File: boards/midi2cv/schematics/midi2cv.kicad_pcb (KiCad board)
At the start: 2 copper layers, 83 x 69 mm, 49 parts, among them J1 Jack-DC (12-32V), U1 LM7805_TO220, U2 6N138, U3 LM358, U4 MCP4822, U5 Pico, U6 LM358

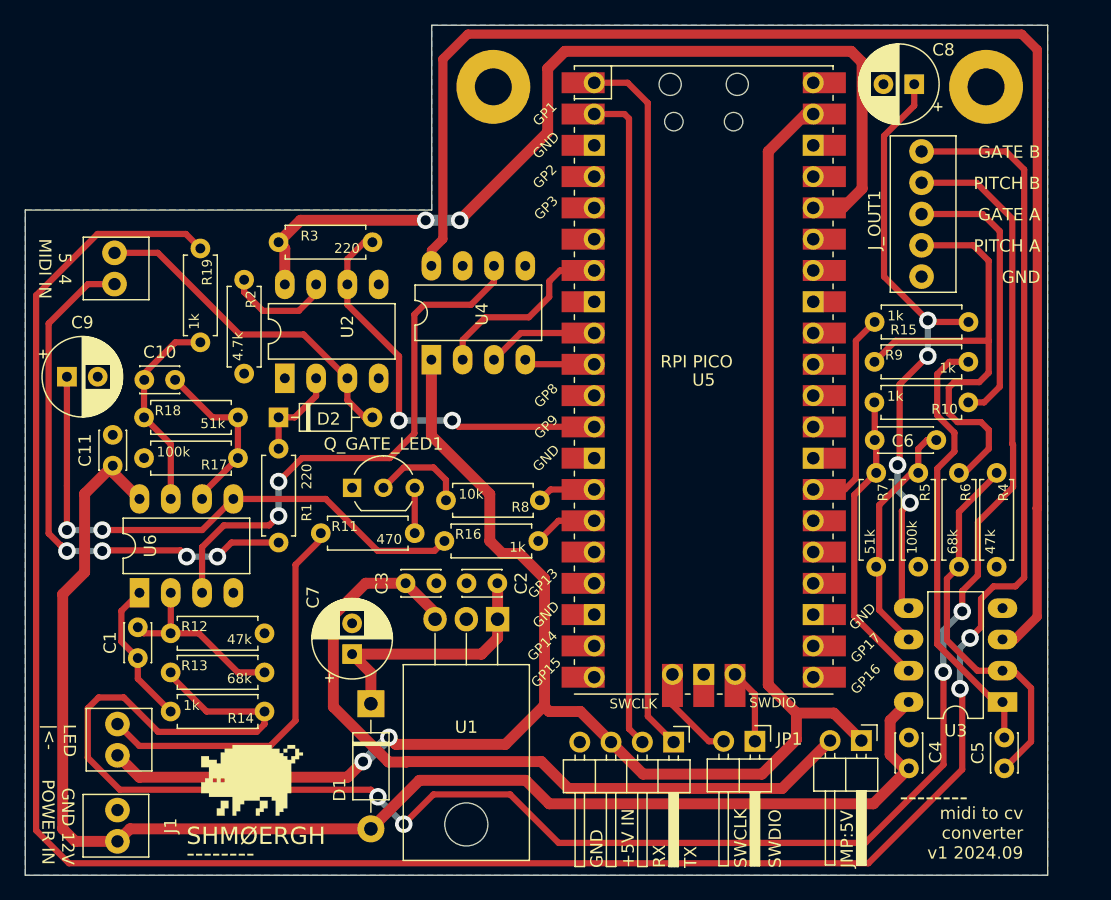
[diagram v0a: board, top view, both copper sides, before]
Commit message: Replaced wired MIDI connection to pins
https://github.com/shmoergh/hog/issues/32

MIDI connection was done with manual wired NTS connectors. Now they are replaced with pins and pinheaders just like the other boards.
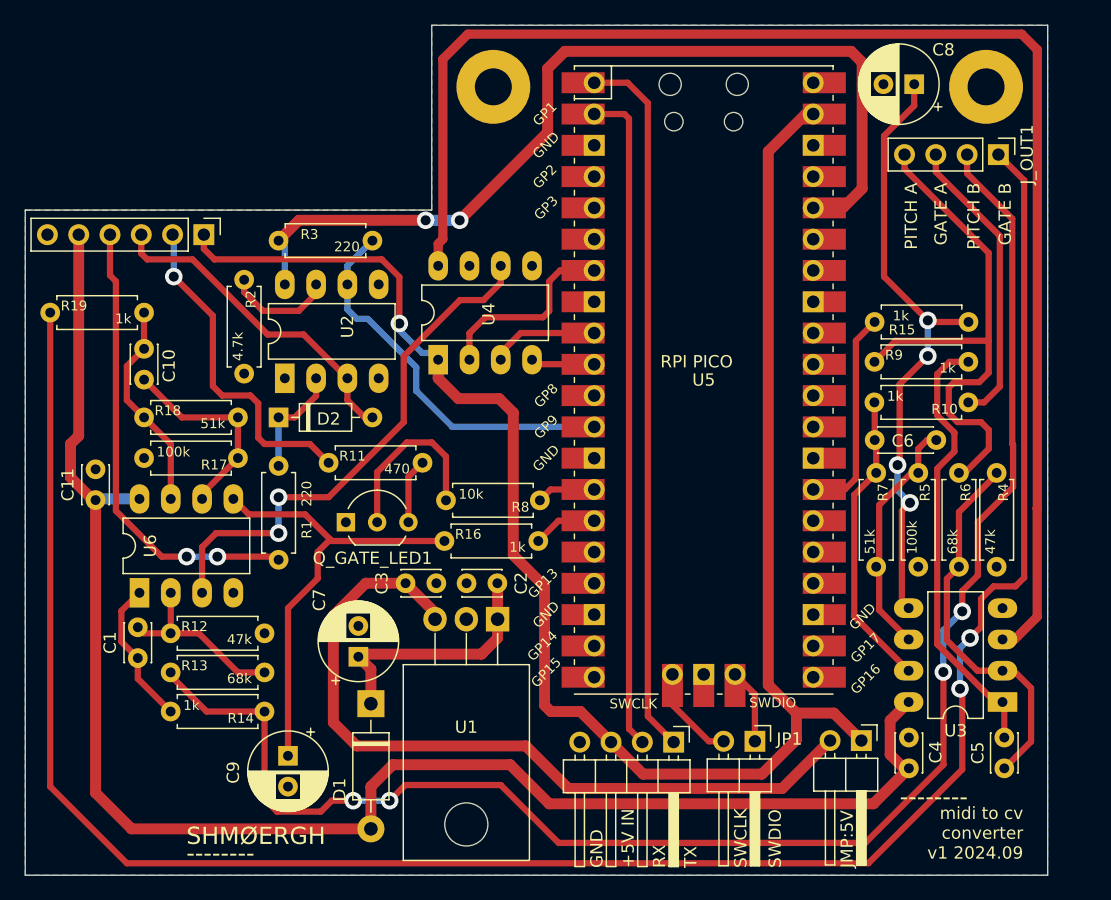
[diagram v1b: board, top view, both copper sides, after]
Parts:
- removed D_LED1: LED, Shmoergh_Custom_Footprints:NSL25_01x02_Vertical
- removed G***: LOGO, Shmoergh_Custom_Footprints:Gyeszno
- removed J1: Jack-DC (12-32V), Shmoergh_Custom_Footprints:NSL25_01x02_Vertical
- removed J_MIDI_IN3.5-7: 3.5mm jack, Shmoergh_Custom_Footprints:NSL25_01x02_Vertical-AudioJack-TS
- added J_IN1: Conn_01x06, Connector_PinHeader_2.54mm:PinHeader_1x06_P2.54mm_Vertical, F.Cu at (85.5, 70.0)
- J_OUT1: value Conn_01x05 -> Conn_01x04; footprint Shmoergh_Custom_Footprints:NSL25_01x05_Vertical -> Connector_PinHeader_2.54mm:PinHeader_1x04_P2.54mm_Vertical
- moved C9 35.6 mm to (92.3, 112.3), turned to -90 degrees
- moved R19 13.3 mm to (73.0, 76.3), turned to 0 degrees
- moved J_OUT1 6.24 mm to (150.0, 63.5)
- moved R11 5.75 mm to (95.6, 88.5)
- moved C11 3.12 mm to (76.7, 91.5)
- moved Q_GATE_LED1 2.84 mm to (97.0, 93.3)
- moved C10 2.52 mm to (80.6, 79.3), turned to -90 degrees
- moved R1 1.40 mm to (91.6, 88.8)
- moved C7 0.55 mm to (98.0, 104.3)
- moved U4 0.55 mm to (104.5, 80.2)
- moved R3 0.13 mm to (91.6, 70.5)
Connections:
- net Net-(D2-A) renamed MIDI_5T
- R1 pad 2: Net-(#J_MIDI_IN1-Pad4) -> MIDI_4R
- R11 pad 1: Net-(D_LED1-K) -> LED_GND
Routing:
- net Net-(#J_MIDI_IN1-Pad4): track 43.7 -> 0.00 mm, vias 4 -> 0
- net MIDI_4R: track 0.00 -> 37.5 mm, vias 0 -> 2
- net Net-(D_LED1-K): track 32.1 -> 0.00 mm
- net PITCH_B: track 162.6 -> 130.6 mm
- net GATE_B: track 199.7 -> 172.3 mm
- net LED_GND: track 0.00 -> 27.3 mm, vias 0 -> 1
- net +12V: track 114.8 -> 130.9 mm
- net +5V: track 154.7 -> 143.8 mm, vias 2 -> 1
- net Net-(U6B-+): track 46.2 -> 37.5 mm, vias 2 -> 0
- net Net-(Q_GATE_LED1-B): track 7.84 -> 14.7 mm
- net PITCH_A: track 40.4 -> 45.3 mm
- net Net-(U6B--): track 14.2 -> 16.7 mm
- net MIDI_IN: track 33.5 -> 31.5 mm, vias 2 -> 0
- net DAC_B: track 44.9 -> 43.1 mm
- net Net-(Q_GATE_LED1-C): track 3.68 -> 5.30 mm
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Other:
- board text added: "12V"
- board text added: "4/S"
- board text added: "5/T"
- board text added: "LED 5V"
- board text added: "LED GND"
- board text removed: "5 4 MIDI IN"
- board text removed: "GND 12V POWER IN"
- board text removed: "LED |<-"

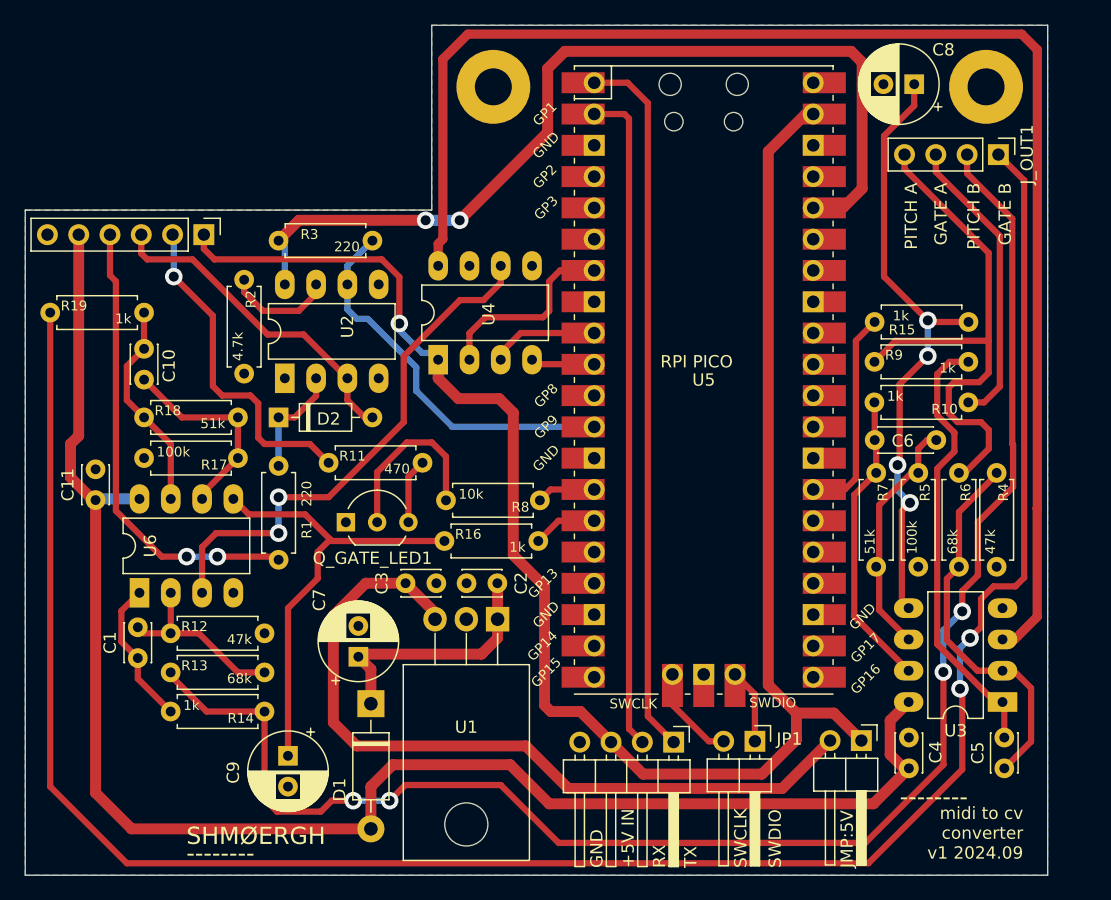
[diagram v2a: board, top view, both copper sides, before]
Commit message: Redesign midi2cv using SMD components
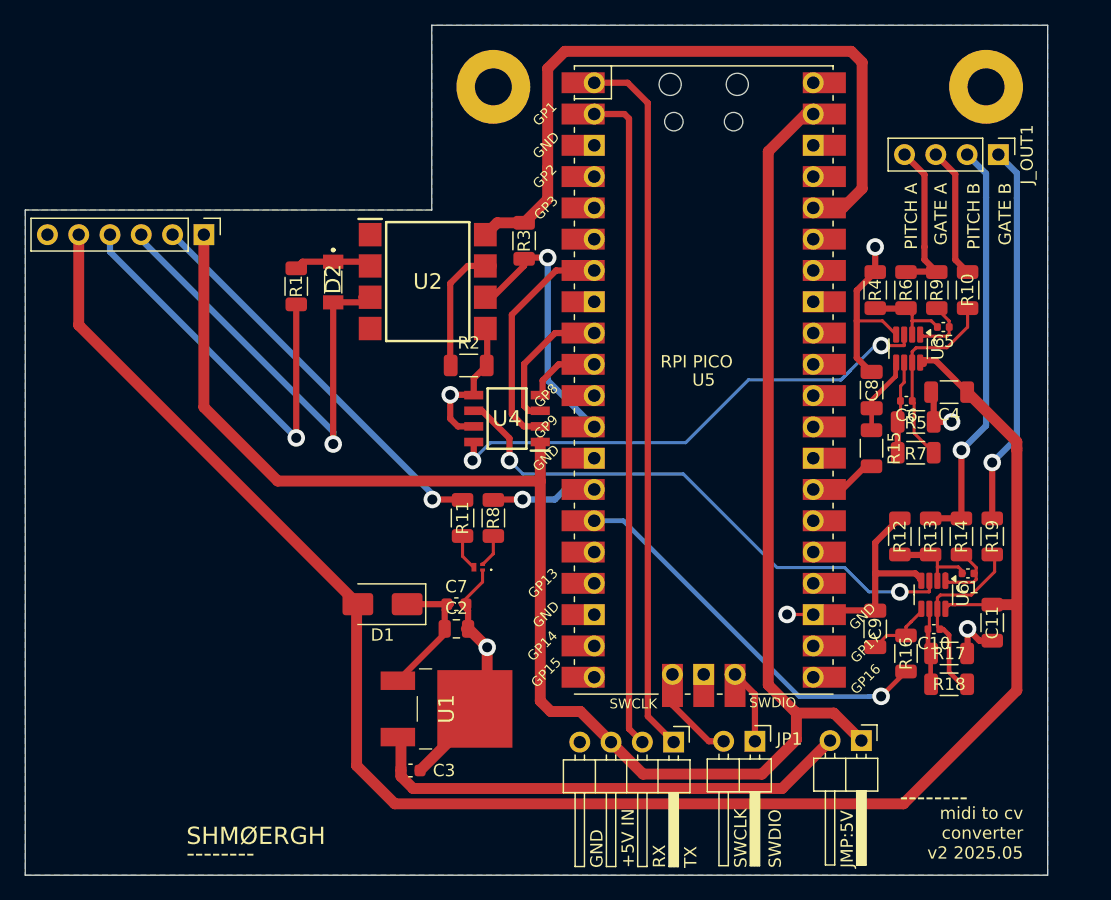
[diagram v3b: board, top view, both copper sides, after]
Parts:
- C1, C10, C5: footprint Capacitor_THT:C_Disc_D3.0mm_W2.0mm_P2.50mm -> Capacitor_SMD:C_0402_1005Metric
- C11, C4: footprint Capacitor_THT:C_Disc_D3.0mm_W2.0mm_P2.50mm -> Resistor_SMD:R_1206_3216Metric
- C2: footprint Capacitor_THT:C_Disc_D3.0mm_W2.0mm_P2.50mm -> Capacitor_SMD:C_0805_2012Metric
- C3: footprint Capacitor_THT:C_Disc_D3.0mm_W2.0mm_P2.50mm -> Capacitor_SMD:C_0603_1608Metric
- C6: footprint Capacitor_THT:C_Disc_D4.3mm_W1.9mm_P5.00mm -> Capacitor_SMD:C_0402_1005Metric
- C7: footprint Capacitor_THT:CP_Radial_D6.3mm_P2.50mm -> Capacitor_SMD:C_0603_1608Metric
- C8, C9: footprint Capacitor_THT:CP_Radial_D6.3mm_P2.50mm -> Capacitor_SMD:C_1206_3216Metric
- D1: value 1N4001 -> S1A; footprint Diode_THT:D_DO-41_SOD81_P10.16mm_Horizontal -> Diode_SMD:D_SMA
- D2: value 1N4148 -> FDLL4148; footprint Diode_THT:D_DO-35_SOD27_P7.62mm_Horizontal -> Shmoergh_Custom_Footprints:FDLL4448
- Q_GATE_LED1: value 2N3904 -> MMBT3904LP-7; footprint Package_TO_SOT_THT:TO-92_Inline_Wide -> Shmoergh_Custom_Footprints:MMBT3904LP7
- R1, R10, R11, R12, R13, R14, R15, R16, R17, R18, R19, R2, R3, R4, R5, R6, R7, R8, R9: footprint Shmoergh_Custom_Footprints:R_Axial_DIN0207_L6.3mm_D2.5mm_P7.62mm_Horizontal -> Resistor_SMD:R_1206_3216Metric
- U1: value LM7805_TO220 -> L7805CDT-TR; footprint Package_TO_SOT_THT:TO-220-3_Horizontal_TabDown -> Shmoergh_Custom_Footprints:L7805CDTTR
- U2: value 6N138 -> 6N138S-TA1; footprint Package_DIP:DIP-8_W7.62mm_LongPads -> Shmoergh_Custom_Footprints:SOP254P1030X508-8N
- U3, U6: footprint Package_DIP:DIP-8_W7.62mm_LongPads -> Package_TO_SOT_SMD:SOT-23-8
- U4: value MCP4822 -> MCP4822-E/SN; footprint Package_DIP:DIP-8_W7.62mm_LongPads -> Shmoergh_Custom_Footprints:SOIC127P600X175-8N
- moved R19 78.6 mm to (149.5, 94.5), turned to -90 degrees
- moved C11 73.5 mm to (149.5, 101.5), turned to -90 degrees
- moved R18 68.9 mm to (146.0, 106.5), turned to 180 degrees
- moved C10 68.0 mm to (144.8, 102.0), turned to 180 degrees
- moved C1 67.7 mm to (147.5, 97.5), turned to 180 degrees
- moved U6 64.4 mm to (144.7, 99.2), turned to -90 degrees
- moved R13 62.7 mm to (144.5, 94.5), turned to -90 degrees
- moved R17 59.9 mm to (146.0, 104.0), turned to 0 degrees
- moved R12 59.7 mm to (142.0, 94.5), turned to 90 degrees
- moved R14 58.3 mm to (147.0, 94.5), turned to -90 degrees
- moved C9 48.8 mm to (140.0, 102.0), turned to 90 degrees
- moved R16 38.6 mm to (142.5, 104.0), turned to -90 degrees
- moved C5 33.7 mm to (145.5, 77.5), turned to 180 degrees
- moved C4 30.7 mm to (146.0, 82.8), turned to 180 degrees
- moved U3 29.7 mm to (142.7, 79.2), turned to -90 degrees
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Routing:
- net GATE_B: track 172.3 -> 31.4 mm, vias 2 -> 1
- net PITCH_B: track 130.6 -> 33.5 mm, vias 4 -> 1
- net GND: track 0.00 -> 75.8 mm, vias 0 -> 6
- net DAC_A: track 116.2 -> 42.2 mm, vias 0 -> 2
- net Net-(U3B-+): track 50.3 -> 6.19 mm, vias 4 -> 0
- net PITCH_A: track 45.3 -> 13.1 mm
- net Net-(U6B-+): track 37.5 -> 5.46 mm
- net Net-(C5-Pad1): track 36.2 -> 5.01 mm
- net GATE_B_TRIG: track 5.22 -> 32.1 mm, vias 0 -> 1
- net Net-(U3A--): track 31.1 -> 6.98 mm
- net Net-(JP1-B): track 63.7 -> 40.1 mm
- net +3.3V: track 75.8 -> 58.2 mm, vias 2 -> 0
- net +12V: track 130.9 -> 148.1 mm
- net GATE_A: track 24.1 -> 10.6 mm
- net Net-(U3B--): track 20.1 -> 7.42 mm
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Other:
- board text added: "midi to cv converter v2 2025.05"
- board text removed: "midi to cv converter v1 2024.09"
